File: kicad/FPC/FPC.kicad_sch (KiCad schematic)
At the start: 2 parts, among them J3 Conn_01x04_Pin, J4 Conn_01x04_Pin

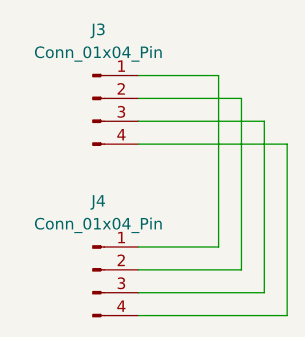
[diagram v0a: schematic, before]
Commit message: 0.960 ソフトウェア＋ドキュメント KiCad v7 基板
普段編集しないモジュールを src/ へ移動し、README を v7 に更新

■ src/ への移動（Arduino IDE のタブ削減）
Arduino IDE はスケッチ直下のファイルを全部タブに出すため 28 個まで増え、
目的のファイルを探しづらくなっていた。仕様が固まっていて普段いじらない
4 モジュールを src/ へ移し、タブを 20 個に減らした。

  src/button.*     ボタン入力・メニュー
  src/sound.*      音声出力（WAV・トーン）
  src/vectormap.*  ベクタ地図の描画
  src/imulog.*     生 IMU ロガー

src/ 配下もコンパイルされるが IDE のタブには出ない。裏を返すと IDE からは
編集できなくなるので、これらは VSCode 等で編集すること。
またスケッチ直下は include パスに入っていないため、src/ の中からルート側の
ヘッダを参照するときは "../mysd.h" のように 1 段戻る必要がある。
この経緯と注意点は GPS_TFT_map.ino のヘッダに残した。

#include は 27 箇所を書き換え、全 104 件が実在するパスへ解決することを確認。

■ 併せて修正
button.cpp の #include "Button.h" が大文字始まりだった。macOS は
ファイルシステムが大文字小文字を区別しないため通っていたが、Linux では
壊れる。"button.h" に修正。

■ README を v7 に更新
 * タイトルとスペックを v7 へ。ソフトウェアバージョン 0.942 → 0.960
 * PONS Link（機体⇄ボート テレメトリ無線）の節を新設。3 台構成、下り一方向に
   した理由、無線パラメータ、実測 350m。設計の詳細は docs/pons_link.md へ
 * BNO085 を β 試験版から標準搭載へ。SPI 接続にした理由も記載
 * マイコンを RP2350B（外付け FLASH 16MB）と明記
 * PCBA とは別に発注する部品の一覧表（Digikey / マルツ / 秋月）を追加
 * 警告音・SD ログ・使用部品に無線関連を追記

重量とバッテリー持続時間は v7 実機での計測待ちのため、v6 β版の参考値と
PONS Link の消費電流だけを記載した。水面での到達距離も未確認と明記。

普段編集しないモジュールを src/ へ移動し、README を v7 に更新

■ src/ への移動（Arduino IDE のタブ削減）
Arduino IDE はスケッチ直下のファイルを全部タブに出すため 28 個まで増え、
目的のファイルを探しづらくなっていた。仕様が固まっていて普段いじらない
4 モジュールを src/ へ移し、タブを 20 個に減らした。

  src/button.*     ボタン入力・メニュー
  src/sound.*      音声出力（WAV・トーン）
  src/vectormap.*  ベクタ地図の描画
  src/imulog.*     生 IMU ロガー

src/ 配下もコンパイルされるが IDE のタブには出ない。裏を返すと IDE からは
編集できなくなるので、これらは VSCode 等で編集すること。
またスケッチ直下は include パスに入っていないため、src/ の中からルート側の
ヘッダを参照するときは "../mysd.h" のように 1 段戻る必要がある。
この経緯と注意点は GPS_TFT_map.ino のヘッダに残した。

#include は 27 箇所を書き換え、全 104 件が実在するパスへ解決することを確認。

■ 併せて修正
button.cpp の #include "Button.h" が大文字始まりだった。macOS は
ファイルシステムが大文字小文字を区別しないため通っていたが、Linux では
壊れる。"button.h" に修正。

■ README を v7 に更新
 * タイトルとスペックを v7 へ。ソフトウェアバージョン 0.942 → 0.960
 * PONS Link（機体⇄ボート テレメトリ無線）の節を新設。3 台構成、下り一方向に
   した理由、無線パラメータ、実測 350m。設計の詳細は docs/pons_link.md へ
 * BNO085 を β 試験版から標準搭載へ。SPI 接続にした理由も記載
 * マイコンを RP2350B（外付け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
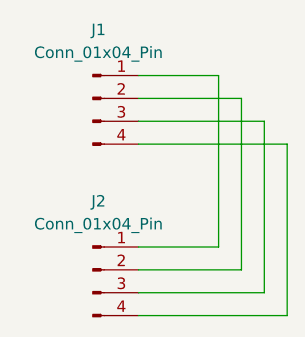
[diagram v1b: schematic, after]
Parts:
- J1: renamed from J3; footprint PONS:FPC_CON 4 POS 1mm -> FPC_CON 4p 1mm:FPC_CON 4p 1mm
- J2: renamed from J4; footprint PONS:FPC_CON 4 POS 1mm -> FPC_CON 4p 1mm:FPC_CON 4p 1mm
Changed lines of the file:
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@@
 (kicad_sch
-	(version 20250114)
+	(version 20260306)
 	(generator "eeschema")
-	(generator_version "9.0")
+	(generator_version "10.0")
 	(paper "A4")
 	(title_block
@@
 		(at 114.3 82.55 0)
 		(unit 1)
+		(body_style 1)
 		(exclude_from_sim no)
 		(in_bom yes)
 		(on_board yes)
+		(in_pos_files yes)
 		(dnp no)
 		(fields_autoplaced yes)
-		(property "Reference" "J3"
+		(property "Reference" "J1"
 			(at 114.935 74.93 0)
+			(show_name no)
+			(do_not_autoplace no)
 			(effects
 				(font
@@
 		(property "Value" "Conn_01x04_Pin"
 			(at 114.935 77.47 0)
-			(effects
-				(font
-					(size 1.27 1.27)
-				)
-			)
-		)
-		(property "Footprint" "PONS:FPC_CON 4 POS 1mm"
+			(show_name no)
+			(do_not_autoplace no)
+			(effects
+				(font
+					(size 1.27 1.27)
+				)
+			)
+		)
+		(property "Footprint" "FPC_CON 4p 1mm:FPC_CON 4p 1mm"
 			(at 114.3 82.55 0)
-			(effects
-				(font
-					(size 1.27 1.27)
-				)
-				(hide yes)
-			)
-		)
-		(property "Datasheet" "~"
+			(hide yes)
+			(show_name no)
+			(do_not_autoplace no)
+			(effects
+				(font
+					(size 1.27 1.27)
+				)
+			)
+		)
+		(property "Datasheet" ""
 			(at 114.3 82.55 0)
-			(effects
-				(font
-					(size 1.27 1.27)
-				)
-				(hide yes)
+			(hide yes)
+			(show_name no)
+			(do_not_autoplace no)
+			(effects
+				(font
+					(size 1.27 1.27)
+				)
 			)
 		)
 		(property "Description" "Generic connector, single row, 01x04, script generated"
 			(at 114.3 82.55 0)
-			(effects
-				(font
-					(size 1.27 1.27)
-				)
-				(hide yes)
+			(hide yes)
+			(show_name no)
+			(do_not_autoplace no)
+			(effects
+				(font
+					(size 1.27 1.27)
+				)
 			)
 		)
@@
 		(at 114.3 101.6 0)
 		(unit 1)
+		(body_style 1)
 		(exclude_from_sim no)
 		(in_bom yes)
 		(on_board yes)
+		(in_pos_files yes)
 		(dnp no)
 		(fields_autoplaced yes)
-		(property "Reference" "J4"
+		(property "Reference" "J2"
 			(at 114.935 93.98 0)
+			(show_name no)
+			(do_not_autoplace no)
 			(effects
 				(font
@@
 		(property "Value" "Conn_01x04_Pin"
 			(at 114.935 96.52 0)
-			(effects
-				(font
-					(size 1.27 1.27)
-				)
-			)
-		)
-		(property "Footprint" "PONS:FPC_CON 4 POS 1mm"
+			(show_name no)
+			(do_not_autoplace no)
+			(effects
+				(font
+					(size 1.27 1.27)
+				)
+			)
+		)
+		(property "Footprint" "FPC_CON 4p 1mm:FPC_CON 4p 1mm"
 			(at 114.3 101.6 0)
-			(effects
-				(font
-					(size 1.27 1.27)
-				)
-				(hide yes)
-			)
-		)
-		(property "Datasheet" "~"
+			(hide yes)
+			(show_name no)
+			(do_not_autoplace no)
+			(effects
+				(font
+					(size 1.27 1.27)
+				)
+			)
+		)
+		(property "Datasheet" ""
 			(at 114.3 101.6 0)
-			(effects
-				(font
-					(size 1.27 1.27)
-				)
-				(hide yes)
+			(hide yes)
+			(show_name no)
+			(do_not_autoplace no)
+			(effects
+				(font
+					(size 1.27 1.27)
+				)
 			)
 		)
 		(property "Description" "Generic connector, single row, 01x04, script generated"
 			(at 114.3 101.6 0)
-			(effects
-				(font
-					(size 1.27 1.27)
-				)
-				(hide yes)
-			)
-		)
+			(hide yes)
+			(show_name no)
+			(do_not_autoplace no)
+			(effects
+				(font
+					(size 1.27 1.27)
+				)
+			)
+		)
